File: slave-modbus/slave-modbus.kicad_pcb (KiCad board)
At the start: 2 copper layers, 25.4 x 72.4 mm, 5 parts, among them J1 Conn_01x06_Male, J2 Conn_01x06_Male, J3 Conn_01x06_Female, J4 Screw_Terminal_01x03, U1 RS485-TTL-Board

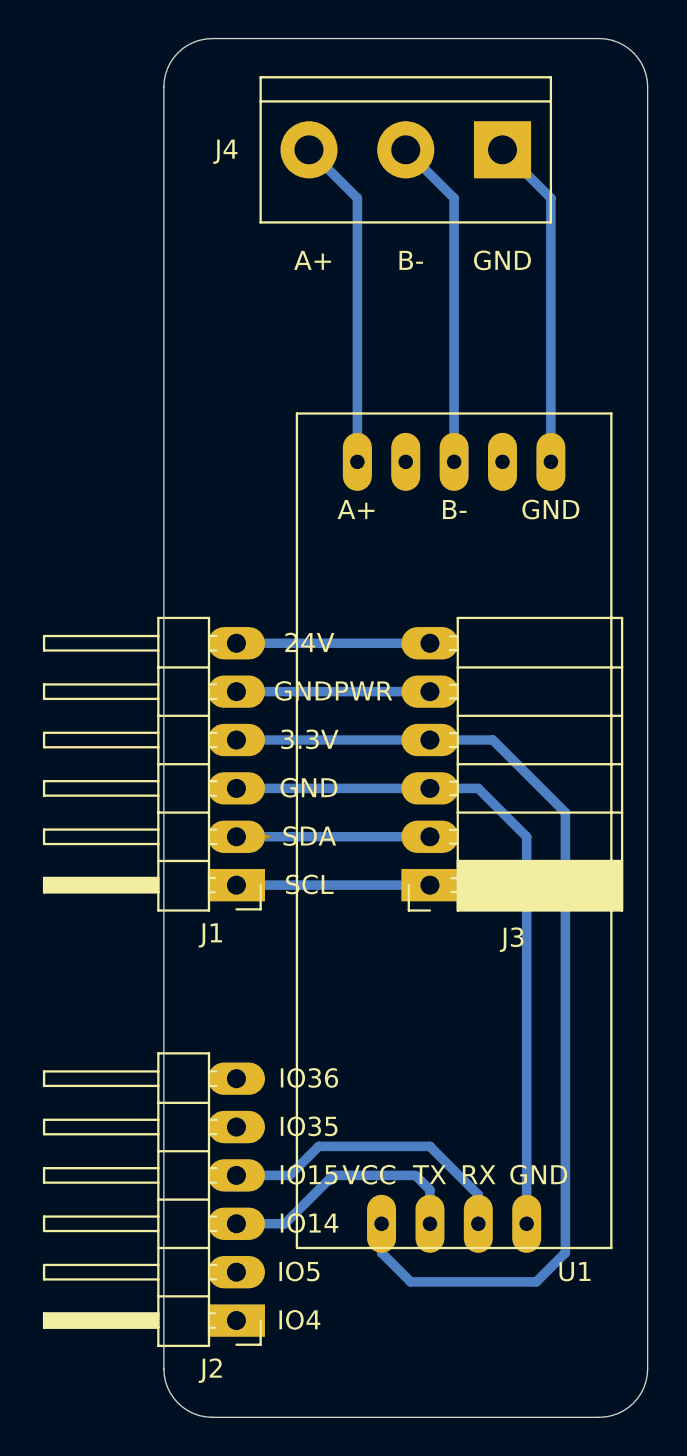
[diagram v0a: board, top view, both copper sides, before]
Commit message: move input/output connectors
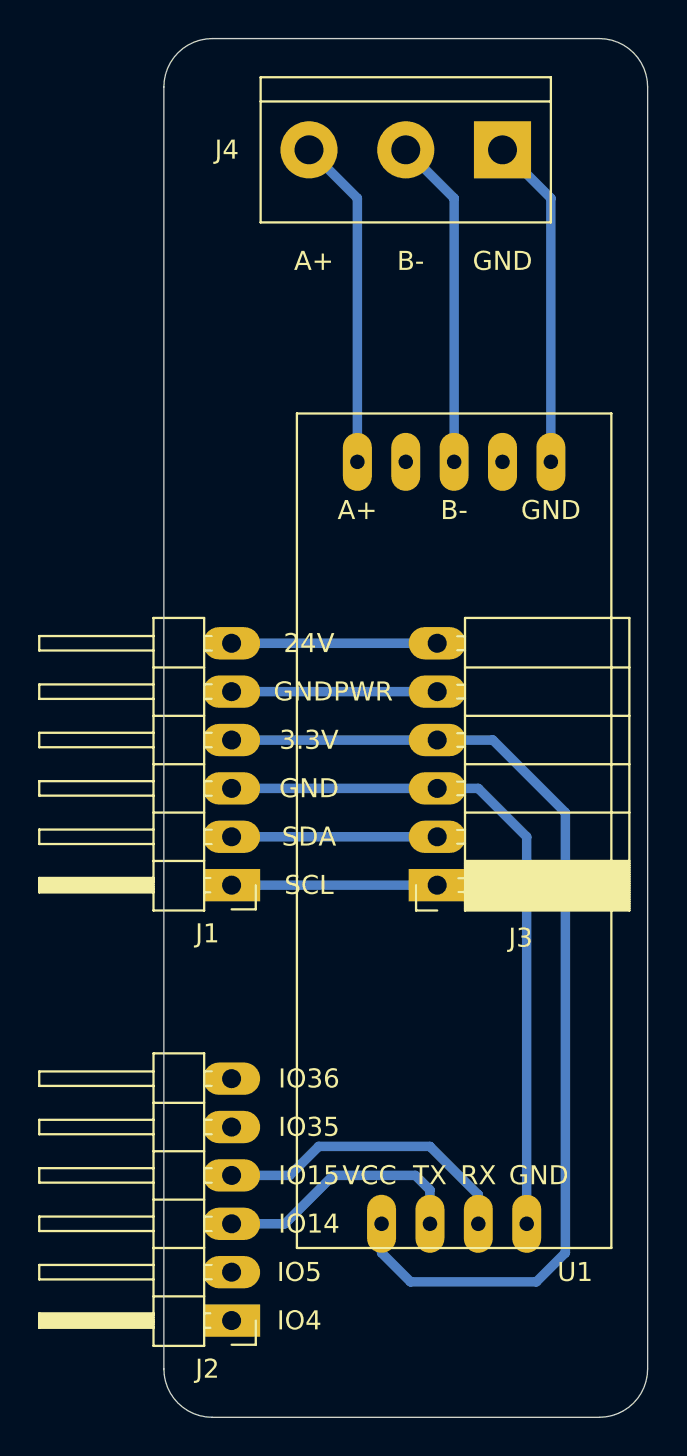
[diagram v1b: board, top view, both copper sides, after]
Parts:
- moved J3 0.38 mm to (77.9, 99.1)
- moved J1 0.25 mm to (67.1, 99.1)
- moved J2 0.25 mm to (67.1, 121.9)
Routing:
- net SDA: track 11.9 -> 10.8 mm
- net SCL: track 10.2 -> 10.8 mm
- net GNDPWR: track 10.2 -> 10.8 mm
- net +24V: track 10.2 -> 10.8 mm

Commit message: slave-modbus - change rs485 board
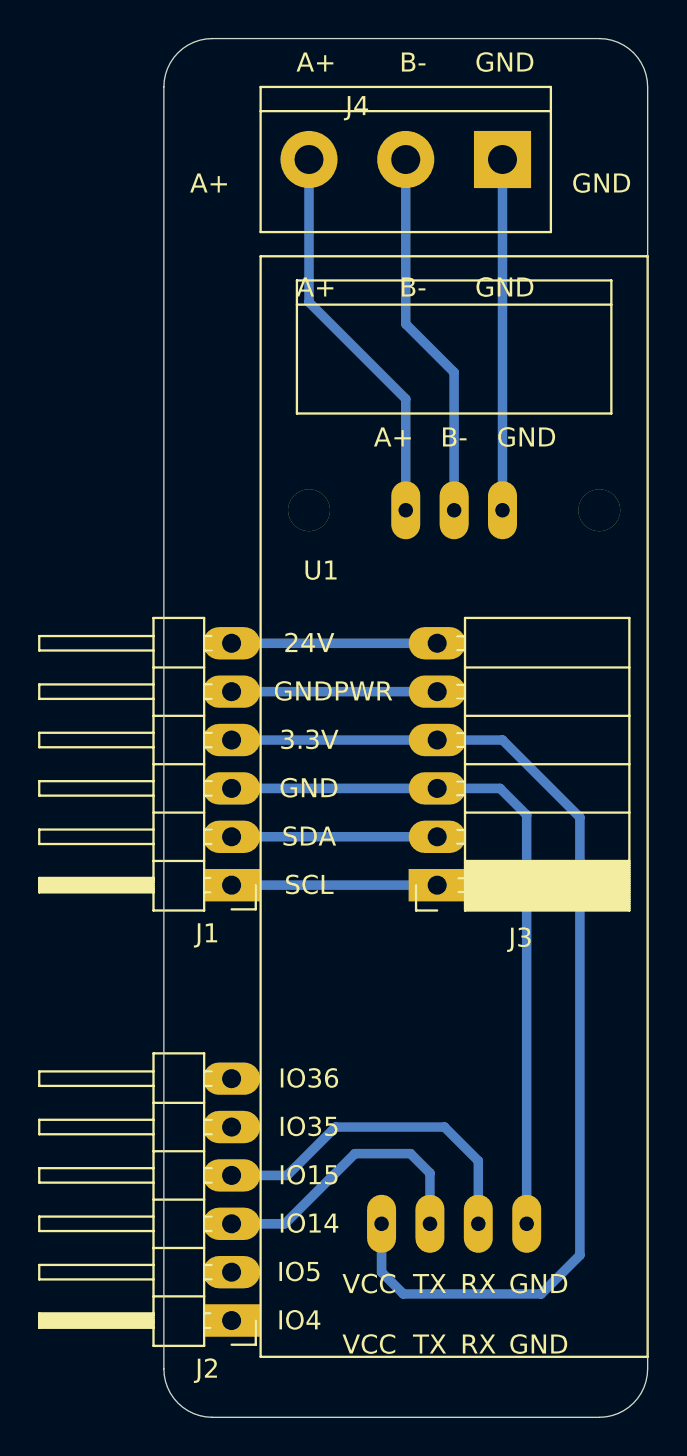
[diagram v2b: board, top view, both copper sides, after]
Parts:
- U1: footprint boards:RS485-TTL-Board -> boards:RS485-TTL-Board-DsdTech
- moved U1 0.63 mm to (78.7, 95.9), turned to 0 degrees
- moved J4 0.51 mm to (81.3, 61.0)
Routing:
- net Net-(J4-Pad3): track 17.4 -> 20.5 mm
- net +3V3: track 54.7 -> 57.2 mm
- net Net-(J4-Pad2): track 17.4 -> 19.5 mm
- net GPIO15: track 16.2 -> 18.0 mm
- net GPIO14: track 13.6 -> 15.0 mm
- net Net-(J4-Pad1): track 17.4 -> 18.4 mm
- net GND: track 36.9 -> 37.5 mm

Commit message: upgrade slave-modbus format
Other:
- net class Default removed
- net class Power removed
